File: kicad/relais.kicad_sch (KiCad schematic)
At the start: 8 parts, among them J10 Screw_Terminal_01x03, J7 Screw_Terminal_01x03, J8 Screw_Terminal_01x03, J9 Screw_Terminal_01x03, K1 RZ03-1C4-D012, K2 RZ03-1C4-D012, K3 RZ03-1C4-D012, K4 RZ03-1C4-D012

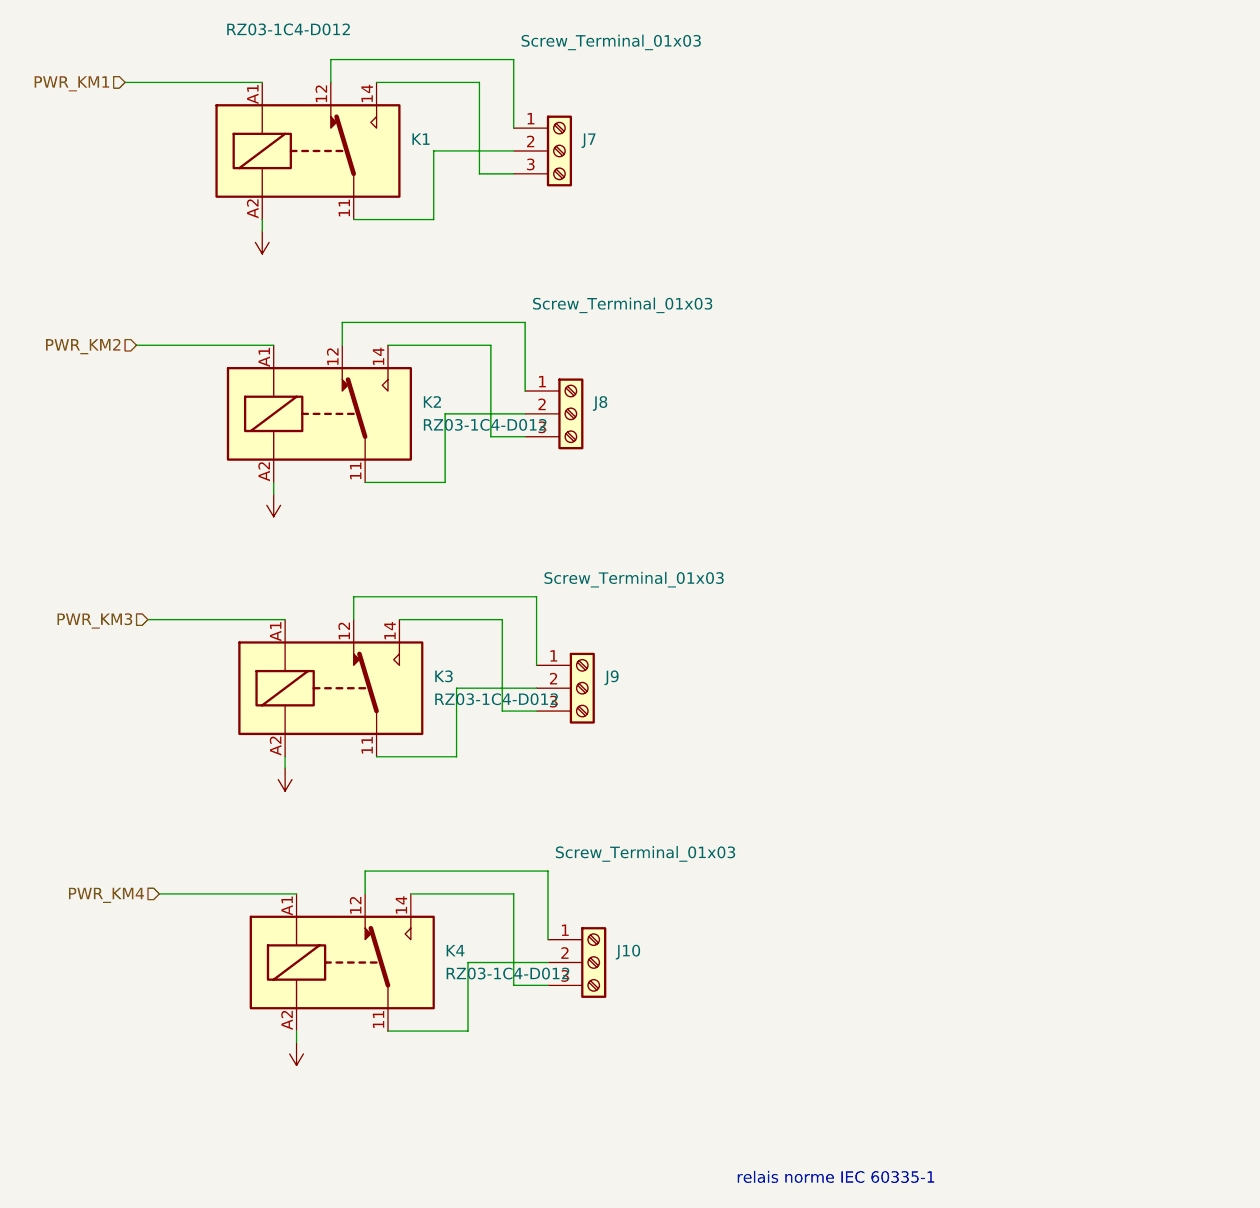
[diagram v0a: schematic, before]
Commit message: minor bug update. add daughter pcb initial commit
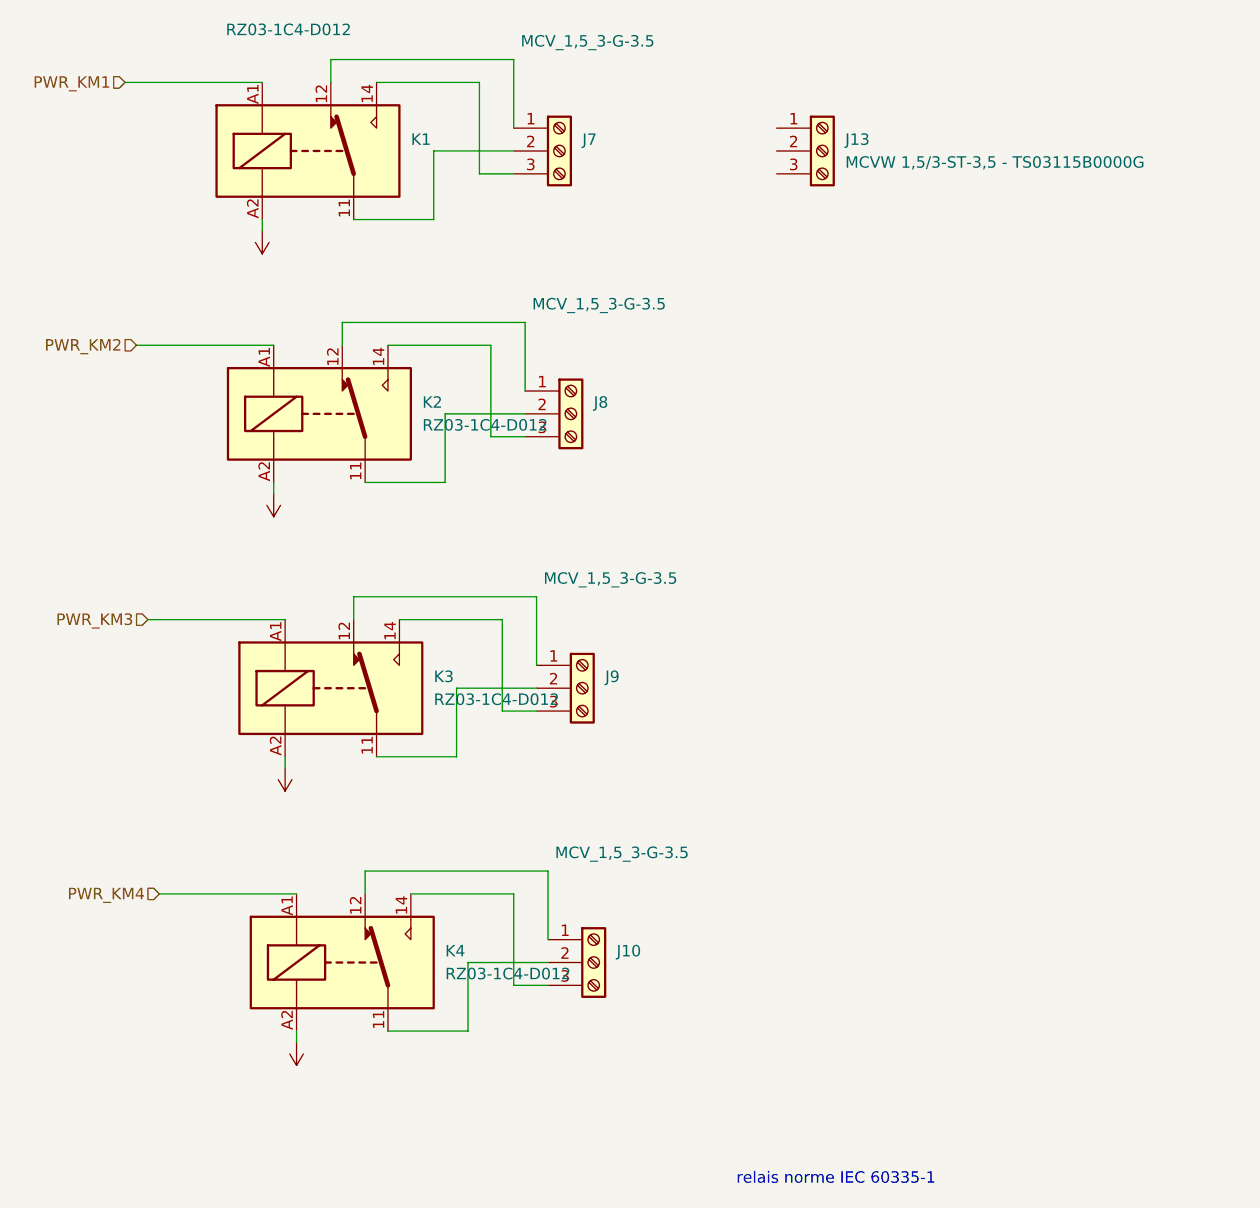
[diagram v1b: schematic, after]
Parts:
- added J13: MCVW 1,5/3-ST-3,5 - TS03115B0000G, symbol Connector:Screw_Terminal_01x03
- J10, J7, J8, J9: value Screw_Terminal_01x03 -> MCV_1,5_3-G-3.5
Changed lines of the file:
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@@
+	)
+	(symbol
+		(lib_id "Connector:Screw_Terminal_01x03")
+		(at 190.5 55.88 0)
+		(unit 1)
+		(exclude_from_sim yes)
+		(in_bom no)
+		(on_board no)
+		(dnp no)
+		(fields_autoplaced yes)
+		(property "Reference" "J13"
+			(at 193.04 54.6099 0)
+			(effects
+				(font
+					(size 1.27 1.27)
+				)
+				(justify left)
+			)
+		)
+		(property "Value" "MCVW 1,5/3-ST-3,5 - TS03115B0000G"
+			(at 193.04 57.1499 0)
+			(effects
+				(font
+					(size 1.27 1.27)
+				)
+				(justify left)
+			)
+		)
+		(property "Footprint" ""
+			(at 190.5 55.88 0)
+			(effects
+				(font
+					(size 1.27 1.27)
+				)
+				(hide yes)
+			)
+		)
+		(property "Datasheet" "~"
+			(at 190.5 55.88 0)
+			(effects
+				(font
+					(size 1.27 1.27)
+				)
+				(hide yes)
+			)
+		)
+		(property "Description" "Generic screw terminal, single row, 01x03, script generated (kicad-library-utils/schlib/autogen/connector/)"
+			(at 190.5 55.88 0)
+			(effects
+				(font
+					(size 1.27 1.27)
+				)
+				(hide yes)
+			)
+		)
+		(pin "3"
+		)
+		(pin "2"
+		)
+		(pin "1"
+		)
+		(instances
+			(project ""
+				(path "/69ed8f4f-6a33-4210-b2ac-8a5f3a02835d/55dce169-37bd-450a-af37-437ce4406a3c"
+					(reference "J13")
+					(unit 1)
+				)
+			)
+		)
 	)
 	(symbol
@@
 			)
 		)
-		(property "Value" "Screw_Terminal_01x03"
+		(property "Value" "MCV_1,5_3-G-3.5"
 			(at 160.782 133.858 0)
 			(effects
@@
 			)
 		)
-		(property "Value" "Screw_Terminal_01x03"
+		(property "Value" "MCV_1,5_3-G-3.5"
 			(at 158.242 72.898 0)
 			(effects
@@
 			)
 		)
-		(property "Value" "Screw_Terminal_01x03"
+		(property "Value" "MCV_1,5_3-G-3.5"
 			(at 156.972 43.688 0)
 			(effects
@@
 			)
 		)
-		(property "Value" "Screw_Terminal_01x03"
+		(property "Value" "MCV_1,5_3-G-3.5"
 			(at 159.512 103.378 0)
 			(effects
